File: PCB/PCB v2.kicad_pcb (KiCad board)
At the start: 4 copper layers, 55 x 42.7 mm, 91 parts, among them J1 Conn_01x02_Pin, J3 6871XX182122_687110182122, J5 Conn_01x03_Pin, J7 Conn_01x07_Pin, U1 LT3483AxS6, U11 OPA4350EA_250, U12 OPA4350EA_250, U13 OPA4350EA_250, U2 LT1761-2.5, U3 LT1964-BYP, U5 AD7606, U6 OPA4350EA_250

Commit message: Prime modifiche
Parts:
- moved R23 8.74 mm to (133.4, 93.2), turned to 180 degrees
- moved R4 1.92 mm to (150.8, 88.3)
- moved C22 1.51 mm to (136.8, 93.2)
- moved D2 1.08 mm to (130.8, 90.7)
- moved R32 1.00 mm to (158.2, 99.0)
- moved R7 0.87 mm to (131.0, 89.0)
- moved C13 0.70 mm to (156.5, 99.0)
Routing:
- net S_sac: track 40.7 -> 69.8 mm
- net S8: track 39.4 -> 52.8 mm
- net out_a1: track 16.6 -> 5.21 mm, vias 2 -> 0
- net -2V5: track 50.1 -> 40.3 mm
- net GND: track 186.3 -> 185.1 mm
- net in-_b1: track 12.3 -> 11.2 mm
- net +2V5: track 33.1 -> 34.2 mm, vias 8 -> 9
- net +5V: track 92.1 -> 91.1 mm, vias 4 -> 3
- net out_b2: track 8.19 -> 7.19 mm
- net S4: track 36.0 -> 35.0 mm
- net Net-(D2-A): track 2.30 -> 1.76 mm
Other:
- board size 55 x 42.7 mm -> 55.3 x 42.7 mm

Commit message: Modifiche accordate fatte
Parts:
- moved J5 42.6 mm to (131.3, 117.1)
- moved R59 3.50 mm to (136.6, 113.5), turned to -45 degrees
- moved H3 2.16 mm to (124.0, 118.0)
- moved H4 2.12 mm to (174.0, 118.0)
- moved H1 0.84 mm to (124.0, 79.0)
- moved H2 0.73 mm to (174.0, 79.0)
- moved R56 0.44 mm to (129.2, 110.0)
- moved R55 0.39 mm to (130.8, 109.9)
- turned R50 to 0 degrees
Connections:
- net BUSY renamed /POWER SUPPLY - ADC - SACRIFIED SENSOR/BUSY
- net CONVST renamed /POWER SUPPLY - ADC - SACRIFIED SENSOR/CONVST
- net RESET renamed /POWER SUPPLY - ADC - SACRIFIED SENSOR/RESET
- net SPI_CS renamed /POWER SUPPLY - ADC - SACRIFIED SENSOR/SPI_CS
- net SPI_MISO renamed /POWER SUPPLY - ADC - SACRIFIED SENSOR/SPI_MISO
- net SPI_SCK renamed /POWER SUPPLY - ADC - SACRIFIED SENSOR/SPI_SCK
- net V_sac renamed /SENSORS/V_sac
- net Vdrive renamed /POWER SUPPLY - ADC - SACRIFIED SENSOR/Vdrive
- net in-_b1 renamed /SENSORS/in-_b1
- net in-_b4 renamed /SENSORS/in-_b4
- net in-_c1 renamed /SENSORS/in-_c1
- net in-_c3 renamed /SENSORS/in-_c3
- net out_a1 renamed /SENSORS/out_a1
- net out_a4 renamed /SENSORS/out_a4
- net out_b1 renamed /SENSORS/out_b1
- net out_b3 renamed /SENSORS/out_b3
- C16 pad 1: out_a3 -> /SENSORS/out_a3
- R47 pad 1: out_a3 -> /SENSORS/out_a3
- R49 pad 1: in-_b3 -> /SENSORS/in-_b3
- R50 pad 1: in-_b3 -> /SENSORS/out_a3
- R50 pad 2: out_a3 -> /SENSORS/in-_b3
- U12 pad 1: out_a3 -> /SENSORS/out_a3
- U12 pad 6: in-_b3 -> /SENSORS/in-_b3
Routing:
- net GND: track 185.1 -> 128.4 mm, vias 35 -> 45
- net S_sac: track 69.8 -> 16.8 mm, vias 2 -> 0
- net S8: track 52.8 -> 15.5 mm, vias 2 -> 0
- net -2V5: track 40.3 -> 28.2 mm
- net in-_b3: track 11.7 -> 0.00 mm
- net /SENSORS/in-_b3: track 0.00 -> 11.6 mm
- net +2V5: track 34.2 -> 27.7 mm, vias 9 -> 10
- net out_a3: track 5.26 -> 0.00 mm
- net /SENSORS/out_a3: track 0.00 -> 4.91 mm
- net /SENSORS/in-_b4: track 6.21 -> 8.93 mm
- net /SENSORS/in-_b1: track 11.2 -> 12.1 mm
- net /SENSORS/out_b1: track 10.8 -> 10.1 mm
- net Net-(U1-FB): track 11.2 -> 10.5 mm
- net /SENSORS/out_a1: track 5.21 -> 4.54 mm
- net Net-(U6-+IN_D): track 12.5 -> 11.8 mm
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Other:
- board size 55.3 x 42.7 mm -> 56 x 45 mm

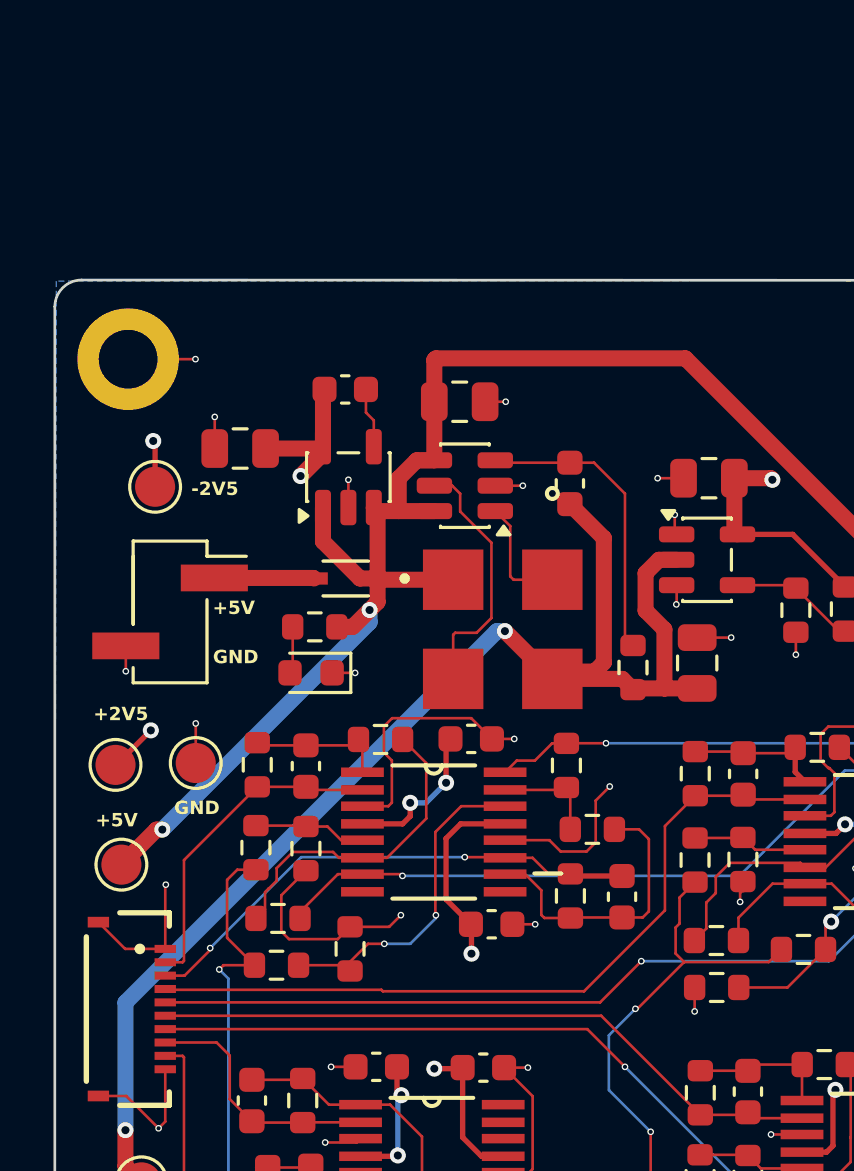
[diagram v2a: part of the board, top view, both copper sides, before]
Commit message: Added decoupling caps to LDOs, started reworking the power SMPS layout
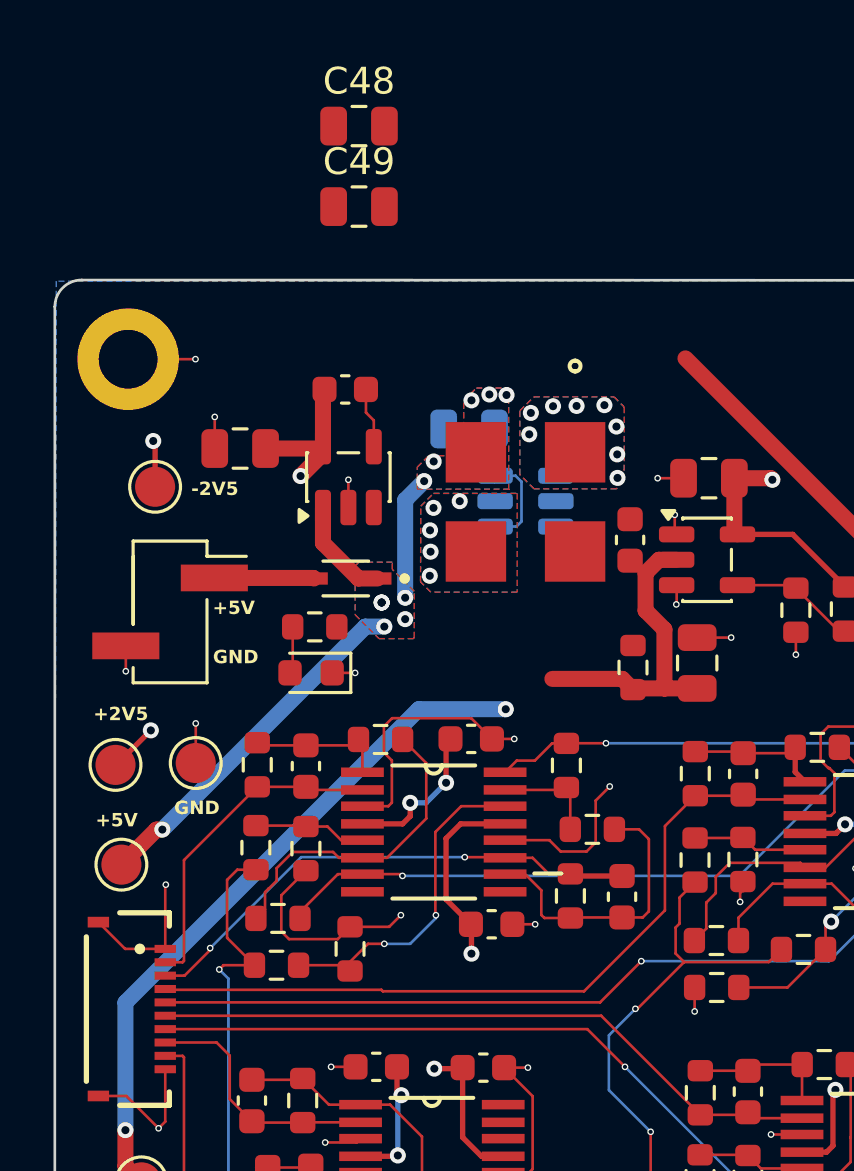
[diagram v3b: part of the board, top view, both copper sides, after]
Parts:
- added C48: 1u, Capacitor_SMD:C_0805_2012Metric, F.Cu at (132.6, 70.3)
- added C49: 1u, Capacitor_SMD:C_0805_2012Metric, F.Cu at (132.6, 73.3)
- C1, U1: moved to B.Cu
- moved L1 4.84 mm to (138.9, 84.3)
- moved C2 3.09 mm to (142.8, 85.8)
- moved U1 2.34 mm to (138.9, 84.3)
- moved C1 1.08 mm to (136.8, 81.6), turned to 180 degrees
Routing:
- net +5V: track 91.0 -> 72.7 mm, vias 2 -> 11
- net -5V: track 49.2 -> 37.2 mm
- net Net-(U1-FB): track 10.5 -> 0.00 mm
- net Net-(U1-D): track 9.56 -> 0.00 mm, vias 0 -> 5
- net Net-(U1-SW): track 4.30 -> 0.00 mm, vias 0 -> 8
- net GND: track 128.4 -> 126.6 mm, vias 45 -> 43
- added copper zone on B.Cu, net +5V
- added copper zone on F.Cu, net +5V
- added copper zone on B.Cu, net Net-(U1-D)
- added copper zone on F.Cu, net Net-(U1-D)
- added copper zone on B.Cu, net Net-(U1-SW)
- added copper zone on F.Cu, net Net-(U1-SW)

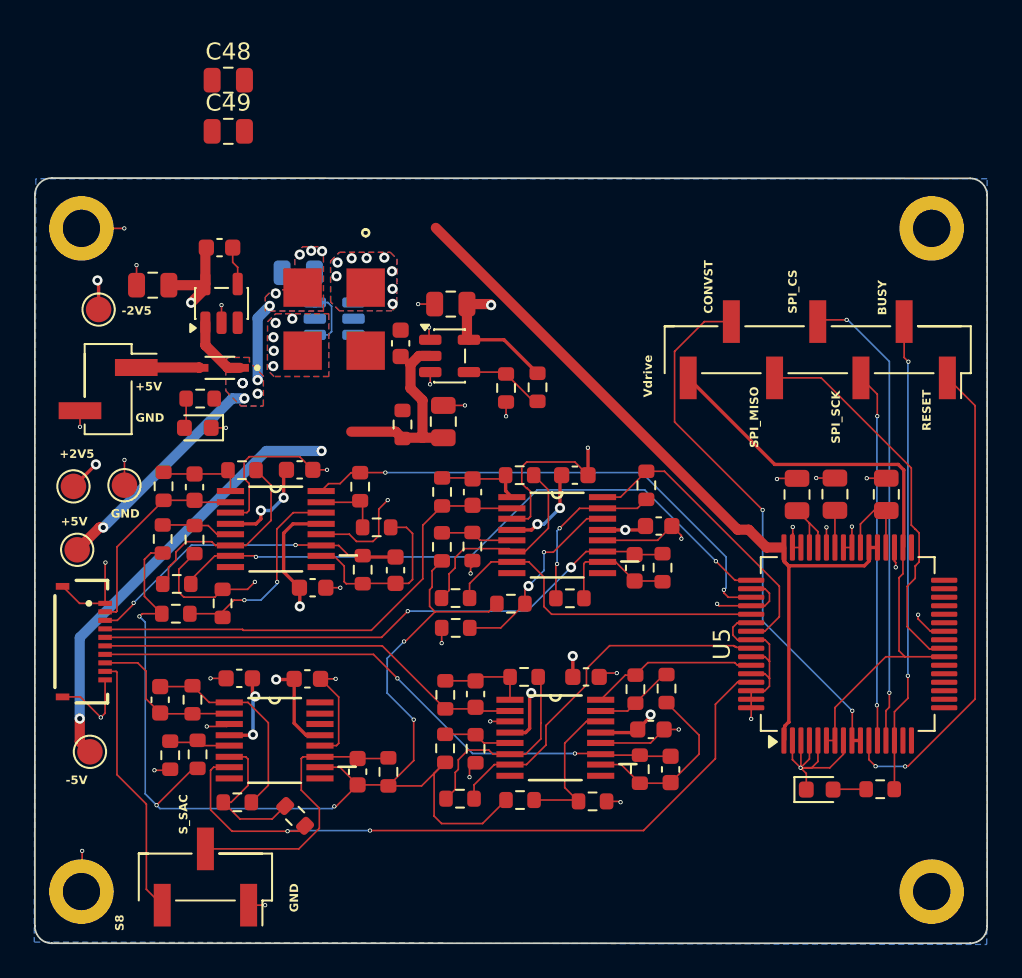
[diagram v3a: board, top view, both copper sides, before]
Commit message: Added decoupling on LDOs, continued optimized power layout, changed packages of 1uF caps
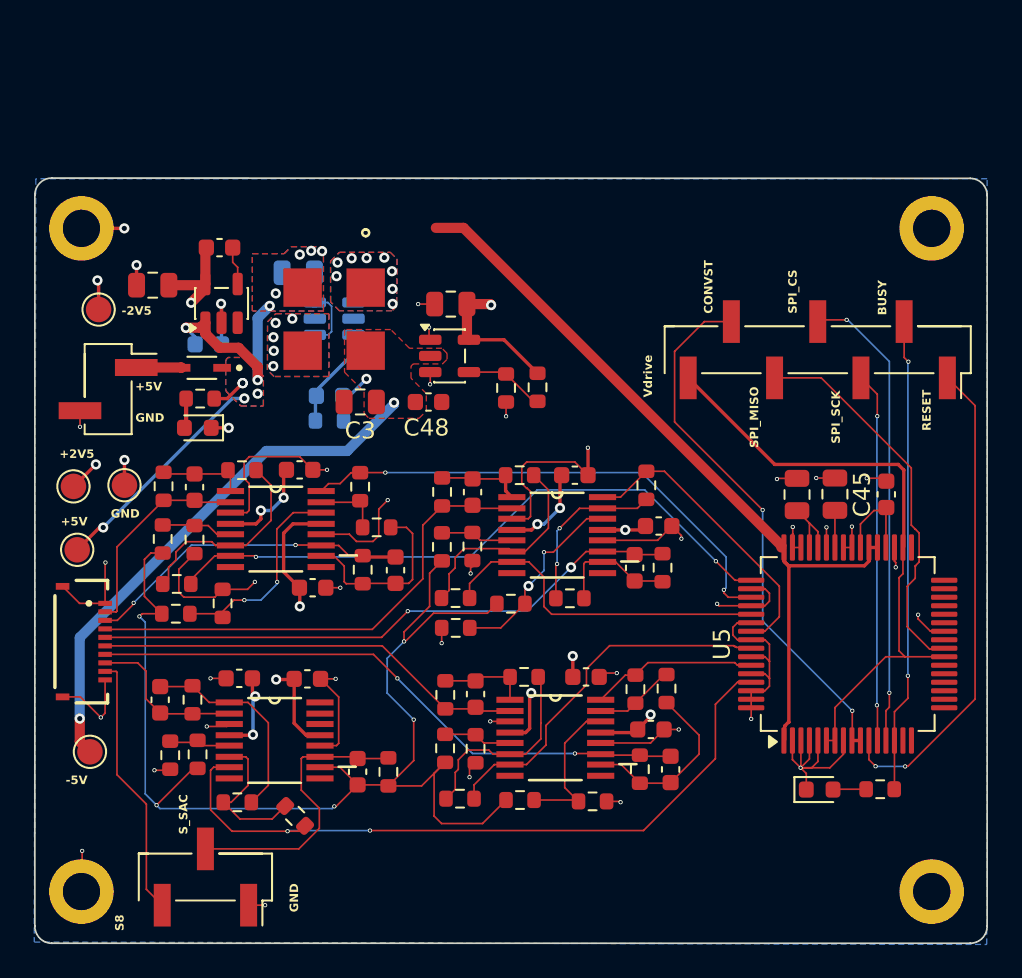
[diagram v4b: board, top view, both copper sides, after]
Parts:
- C2, R3: moved to B.Cu
- C45, C48: footprint Capacitor_SMD:C_0805_2012Metric -> Capacitor_SMD:C_0603_1608Metric
- C49: footprint Capacitor_SMD:C_0805_2012Metric -> Capacitor_SMD:C_0603_1608Metric; moved to B.Cu
- moved C48 22.3 mm to (144.4, 89.2)
- moved C49 12.6 mm to (131.5, 85.8)
- moved C2 5.20 mm to (138.6, 88.8), turned to 180 degrees
- moved C3 5.02 mm to (140.4, 89.2), turned to 180 degrees
- moved R3 4.30 mm to (138.6, 90.3), turned to 180 degrees
- moved D1 1.06 mm to (131.1, 87.2)
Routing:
- net Net-(U1-FB): track 0.00 -> 5.98 mm
- net +5V: track 72.7 -> 78.6 mm, vias 11 -> 12
- net -5V: track 37.2 -> 34.5 mm, vias 2 -> 3
- net /SENSORS/V_sac: track 70.0 -> 72.2 mm
- net GND: track 126.6 -> 128.0 mm, vias 43 -> 42
- net Net-(J1-Pin_1): track 3.73 -> 2.67 mm
- added copper zone on F.Cu, net -5V

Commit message: Changed power, started changing ADC and refactoring signal amplitude
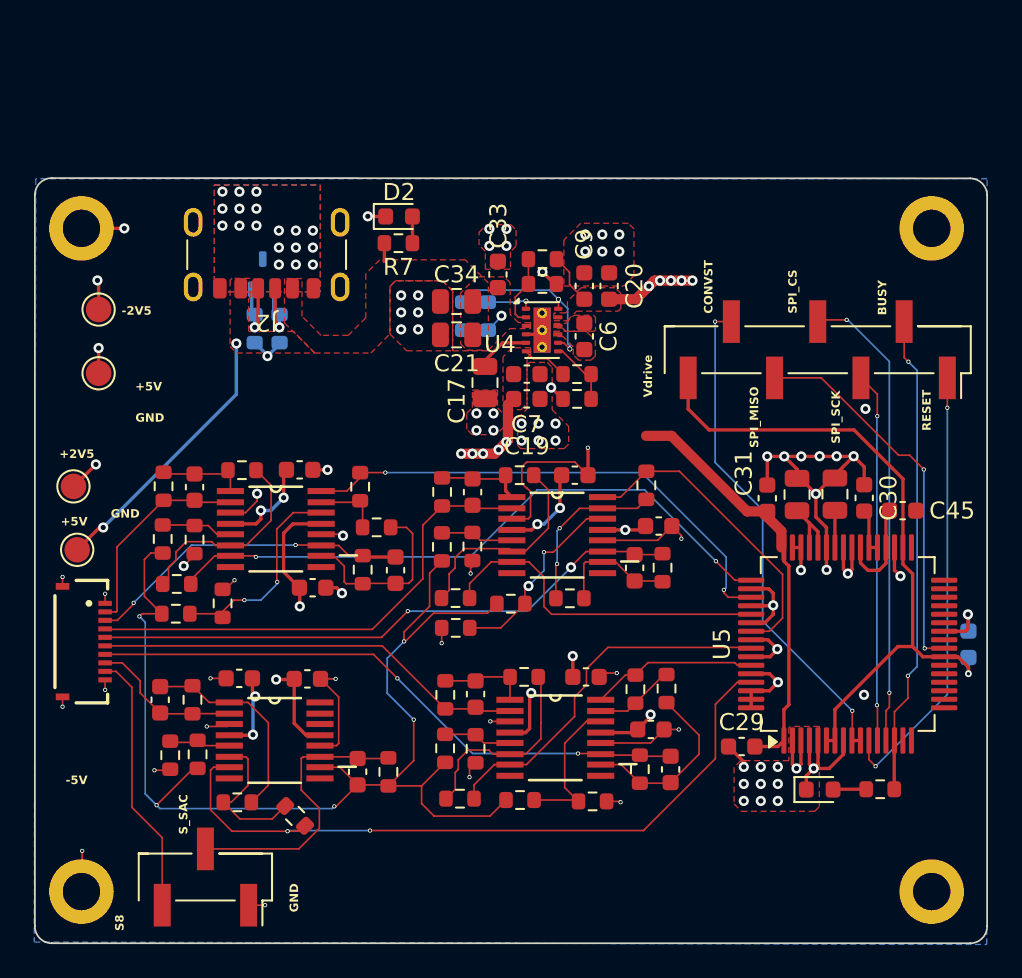
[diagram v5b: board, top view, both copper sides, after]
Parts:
- removed C1: 4.7u, Capacitor_SMD:C_0805_2012Metric
- removed C2: 22p, Capacitor_SMD:C_0603_1608Metric
- removed C3, C4, C42: 10u, Capacitor_SMD:C_0805_2012Metric
- removed C48, C49: 1u, Capacitor_SMD:C_0603_1608Metric
- removed C5: 0.01u, Capacitor_SMD:C_0603_1608Metric
- removed D1: BAT760-7, BAT760-7 diodo:SOD2513X120N
- removed J1: Conn_01x02_Pin, Connector_PinHeader_2.54mm:PinHeader_1x02_P2.54mm_Vertical_SMD_Pin1Right
- removed L1: SDQ12-4R7-R, COILTRONICS SDQ12-4R7 INDUTTORI ACCOPPIATI:INDM5252X12N
- removed R5: 100k, Resistor_SMD:R_0603_1608Metric
- removed TP4: TestPoint, TestPoint:TestPoint_Pad_D1.5mm
- removed U2: LT1761-2.5, Package_TO_SOT_SMD:TSOT-23-5
- removed U3: LT1964-BYP, Package_TO_SOT_SMD:TSOT-23-5
- added C17: 10u, Capacitor_SMD:C_0805_2012Metric, F.Cu at (147.7, 88.1)
- added C19: 4.7u, Capacitor_SMD:C_0603_1608Metric, F.Cu at (150.2, 89.0)
- added C20: 4.7u, Capacitor_SMD:C_0603_1608Metric, F.Cu at (155.0, 82.4)
- added C21: 10u, Capacitor_SMD:C_0805_2012Metric, F.Cu at (146.1, 85.3)
- added C29: 100n, Capacitor_SMD:C_0603_1608Metric, F.Cu at (162.8, 109.5)
- added C30: 100n, Capacitor_SMD:C_0603_1608Metric, F.Cu at (170.0, 94.8)
- added C31: 100n, Capacitor_SMD:C_0603_1608Metric, F.Cu at (164.3, 94.9)
- added C32: 100n, Capacitor_SMD:C_0603_1608Metric, B.Cu at (176.2, 103.5)
- added C33: 100n, Capacitor_SMD:C_0603_1608Metric, F.Cu at (148.5, 81.7)
- added C34: 10u, Capacitor_SMD:C_0805_2012Metric, F.Cu at (146.1, 83.3)
- added C6: 1u, Capacitor_SMD:C_0603_1608Metric, F.Cu at (153.6, 85.3)
- added C7: 100n, Capacitor_SMD:C_0603_1608Metric, F.Cu at (150.2, 87.6)
- added C9: 100n, Capacitor_SMD:C_0603_1608Metric, F.Cu at (153.6, 82.4)
- added J2: USB_C_Receptacle_PowerOnly_6P, Connector_USB:USB_C_Receptacle_GCT_USB4125-xx-x_6P_TopMnt_Horizontal, F.Cu at (134.9, 79.4)
- added R1: 130k, PCM_SparkFun-Resistor:R_0603_1608Metric, F.Cu at (151.1, 80.8)
- added R11: 10k, PCM_SparkFun-Resistor:R_0603_1608Metric, B.Cu at (147.9, 84.2)
- added R12: 10k, PCM_SparkFun-Resistor:R_0603_1608Metric, B.Cu at (146.4, 84.2)
- added R2: 105k, PCM_SparkFun-Resistor:R_0603_1608Metric, F.Cu at (153.1, 87.6)
- added R6: 120k, PCM_SparkFun-Resistor:R_0603_1608Metric, F.Cu at (151.1, 82.3)
- added R9: 100k, PCM_SparkFun-Resistor:R_0603_1608Metric, F.Cu at (153.1, 89.0)
- added U4: LM27762, Package_SON:WSON-12-1EP_3x2mm_P0.5mm_EP1x2.65_ThermalVias, F.Cu at (151.1, 85.0)
- R3: value 511k -> 5.1k; footprint Resistor_SMD:R_0603_1608Metric -> PCM_SparkFun-Resistor:R_0603_1608Metric
- R4: value 105k -> 5.1k; footprint Resistor_SMD:R_0603_1608Metric -> PCM_SparkFun-Resistor:R_0603_1608Metric; moved to B.Cu
- U1: value LT3483AxS6 -> TPD2E2U06DCK; footprint Package_TO_SOT_SMD:TSOT-23-6 -> Package_TO_SOT_SMD:SOT-323_SC-70
- moved D2 17.2 mm to (142.7, 78.3), turned to 0 degrees
- moved R4 15.6 mm to (135.7, 84.9), turned to -90 degrees
- moved R7 14.8 mm to (142.6, 79.9), turned to 0 degrees
- moved R3 6.98 mm to (134.2, 84.9), turned to -90 degrees
- moved TP5 6.75 mm to (125.0, 87.5)
- moved U1 4.95 mm to (134.7, 81.7), turned to 90 degrees
- moved C45 1.36 mm to (172.3, 95.6), turned to 0 degrees
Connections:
- R3 pad 1: -5V -> Net-(J2-CC2)
- R3 pad 2: Net-(U1-FB) -> GND
- R4 pad 1: Net-(U3-ADJ) -> Net-(J2-CC1)
- R4 pad 2: -2V5 -> GND
- U1 pad 1: Net-(U1-SW) -> Net-(J2-CC1)
- U1 pad 2: GND -> Net-(J2-CC2)
- U1 pad 3: Net-(U1-FB) -> GND
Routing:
- net -5V: track 34.5 -> 0.00 mm, vias 3 -> 0
- net +5V: track 78.6 -> 47.5 mm, vias 12 -> 3
- net GND: track 128.0 -> 115.7 mm, vias 42 -> 103
- net Net-(U4-EN+): track 0.00 -> 10.7 mm, vias 0 -> 2
- net Net-(U1-FB): track 5.98 -> 0.00 mm
- net Net-(J2-CC1): track 0.00 -> 4.79 mm, vias 0 -> 1
- net Net-(J2-CC2): track 0.00 -> 4.70 mm, vias 0 -> 1
- net Net-(U3-ADJ): track 4.35 -> 0.00 mm
- net Net-(U4-FB+): track 0.00 -> 4.26 mm
- net Net-(U4-FB-): track 0.00 -> 3.95 mm
- net /POWER SUPPLY - ADC - SACRIFIED SENSOR/Vdrive: track 36.2 -> 39.8 mm, vias 0 -> 1
- net Net-(U4-CP): track 0.00 -> 3.19 mm
- net +2V5: track 27.7 -> 30.7 mm, vias 10 -> 14
- net Net-(U4-PGOOD): track 0.00 -> 2.71 mm, vias 0 -> 1
- net Net-(J1-Pin_1): track 2.67 -> 0.00 mm
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- added copper zone on F.Cu, net +2V5
- added copper zone on F.Cu, net -2V5
- added copper zone on B.Cu, net GND
- added copper zone on F.Cu, net GND
- added copper zone on F.Cu, net Net-(U4-C+)
- added copper zone on F.Cu, net Net-(U4-C-)
- removed copper zone on B.Cu, net +5V
- removed copper zone on F.Cu, net -5V
- removed copper zone on B.Cu, net Net-(U1-D)
- removed copper zone on F.Cu, net Net-(U1-D)
- removed copper zone on B.Cu, net Net-(U1-SW)
- removed copper zone on F.Cu, net Net-(U1-SW)
